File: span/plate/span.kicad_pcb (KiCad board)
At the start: 2 copper layers, 112 x 95.6 mm, 23 parts, among them SW19 SW_PUSH, SW20 SW_PUSH, SW21 SW_PUSH, SW22 SW_PUSH, SW23 SW_PUSH, SW24 SW_PUSH, SW25 SW_PUSH, SW26 SW_PUSH, SW27 SW_PUSH, SW28 SW_PUSH, SW29 SW_PUSH, SW30 SW_PUSH, SW31 SW_PUSH, SW32 SW_PUSH, SW33 SW_PUSH, SW34 SW_PUSH, SW35 SW_PUSH, SW36 SW_PUSH

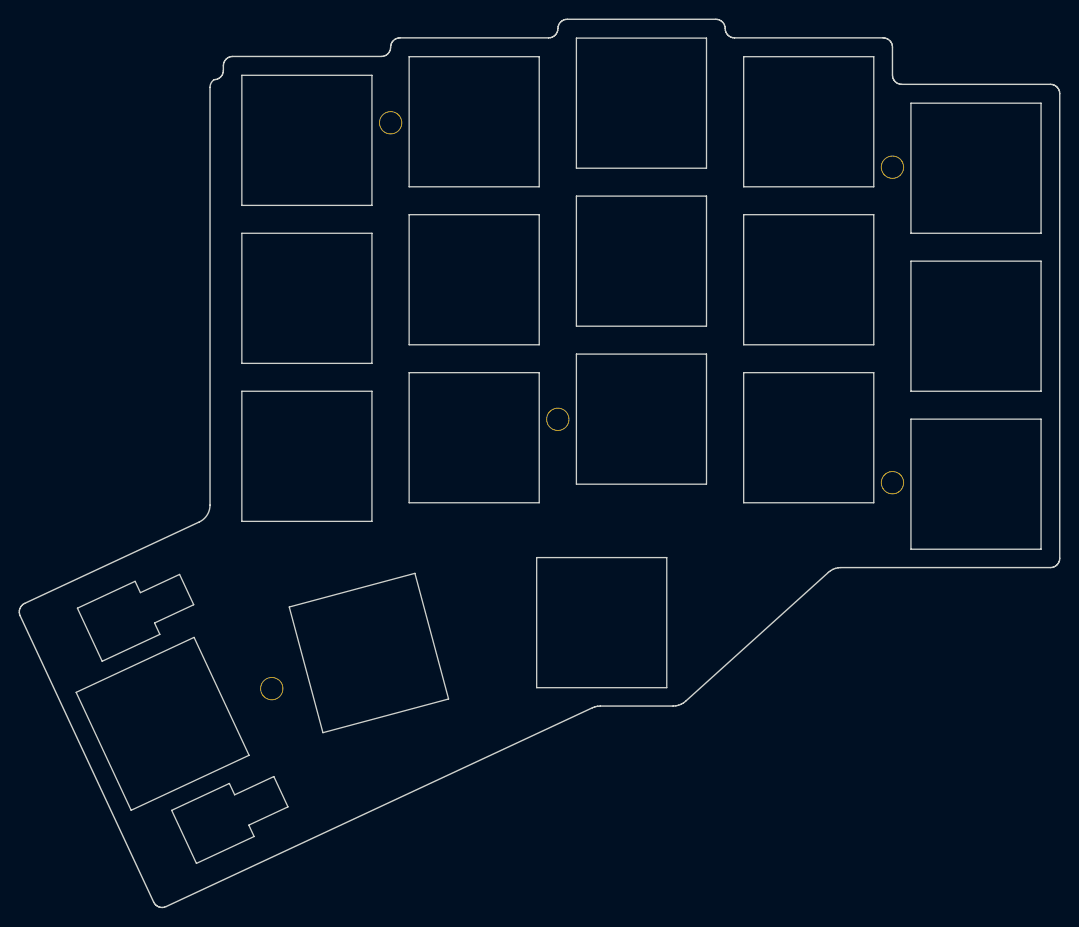
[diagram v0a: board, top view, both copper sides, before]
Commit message: span: move 2 of the thumb keys a bit
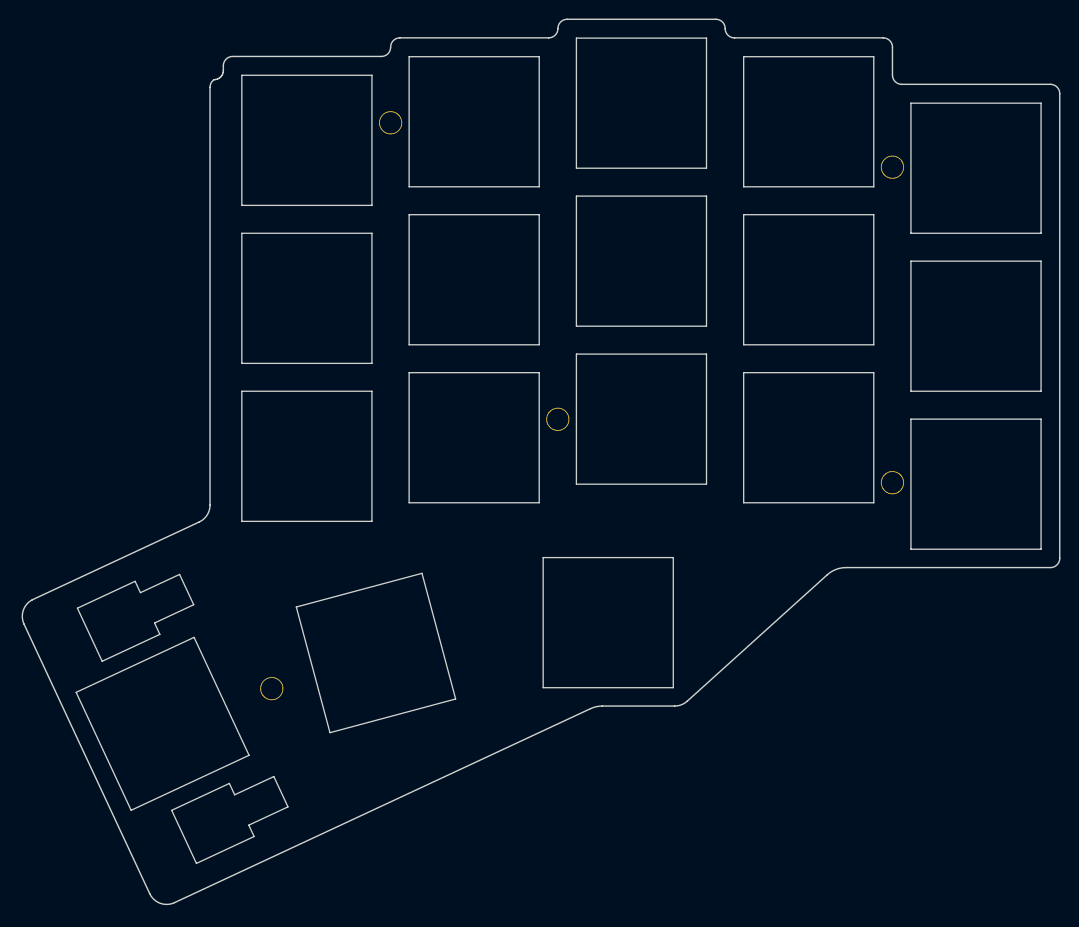
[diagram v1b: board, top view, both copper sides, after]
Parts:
- moved SW35 0.76 mm to (174.0, 105.6)
- moved SW34 0.70 mm to (199.0, 102.3)
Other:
- board size 112 x 95.6 mm -> 111.6 x 95.2 mm
